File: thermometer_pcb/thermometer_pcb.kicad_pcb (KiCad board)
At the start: 2 copper layers, 76.6 x 49 mm, 18 parts, among them J1 POWER_IN, J2 TC_IN, J3 EXT_DS1, J4 EXT_DS2, J5 DISP, J6 Conn_01x02, Q1 PN2222A, U1 DS18B20

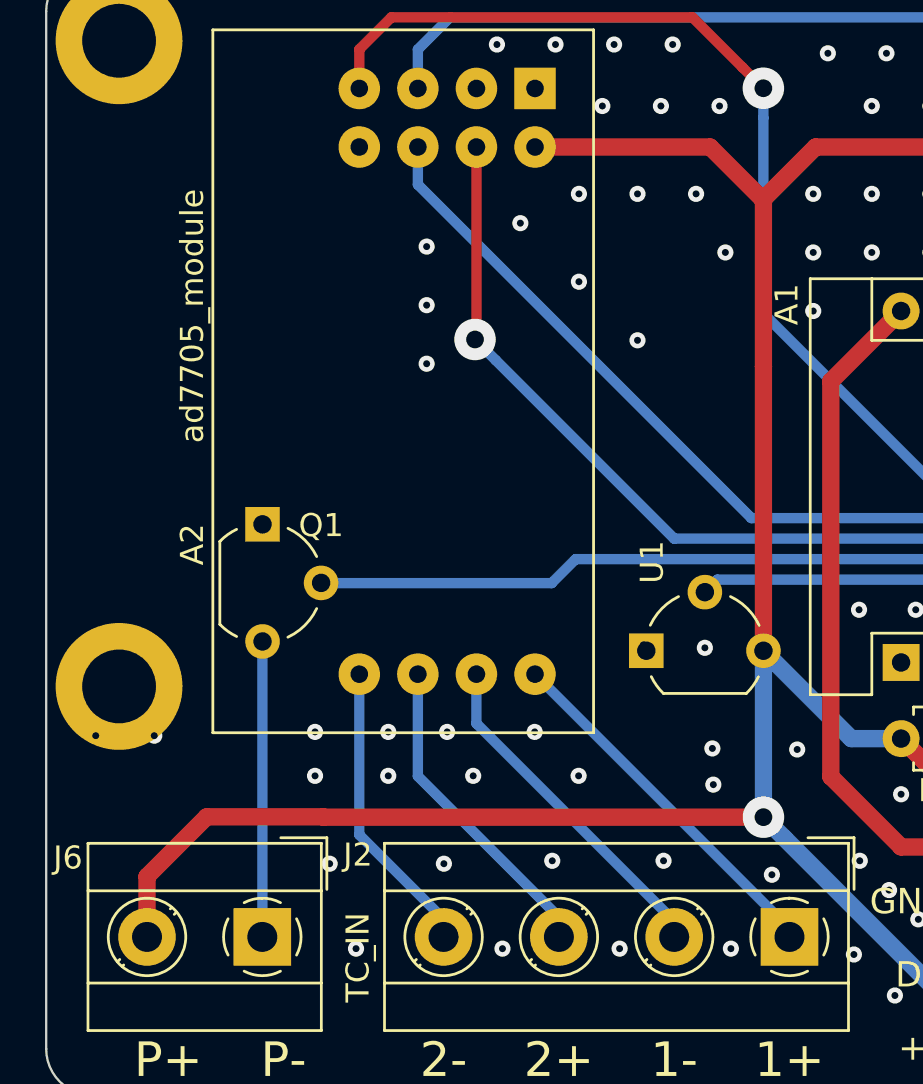
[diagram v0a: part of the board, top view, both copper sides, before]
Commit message: pcb: reroute PID+ track
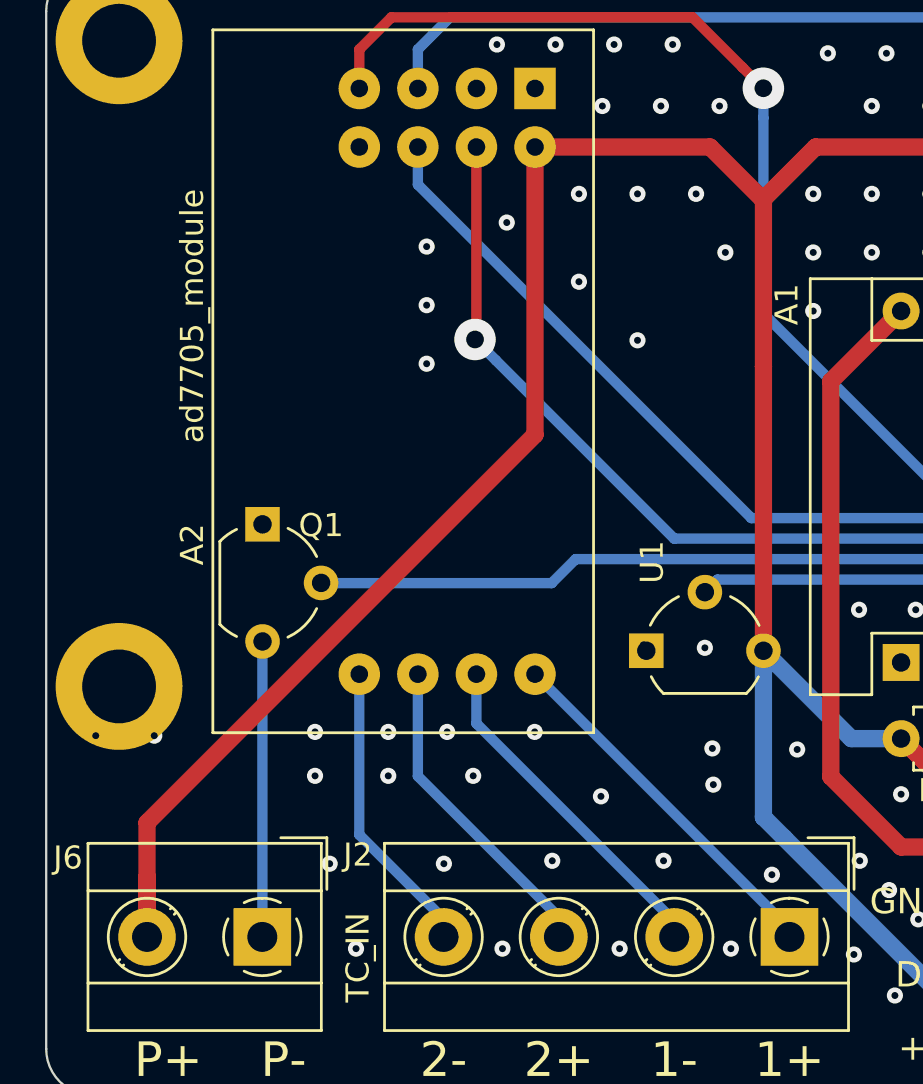
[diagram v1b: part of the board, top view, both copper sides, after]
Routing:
- net +5V: track 167.5 -> 180.9 mm, vias 1 -> 0
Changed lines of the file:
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@@
     (thickness 1.6)
     (drawings 60)
-    (tracks 272)
+    (tracks 270)
     (modules 18)
     (nets 20)
@@
   (gr_line (start 222.221676 76.190177) (end 222.221676 46.018604) (layer "Edge.Cuts") (width 0.1))
   (gr_arc (start 220.221676 46.018604) (end 222.221676 46.018604) (angle -90) (layer "Edge.Cuts") (width 0.1))
+  (segment (start 166.833677 64.382604) (end 150.008677 81.207604) (width 0.75) (layer "F.Cu") (net 2))
+  (segment (start 166.833677 51.906604) (end 166.833677 64.382604) (width 0.75) (layer "F.Cu") (net 2))
+  (segment (start 150.008677 81.207604) (end 150.008677 86.160604) (width 0.75) (layer "F.Cu") (net 2))
+  (via micro (at 169.693677 80.064604) (size 0.7) (drill 0.3) (layers "F.Cu" "B.Cu") (net 1))
+  (via micro (at 165.608667 55.182605) (size 0.7) (drill 0.3) (layers "F.Cu" "B.Cu") (net 1))
   (segment (start 199.208677 87.252604) (end 208.885477 77.575804) (width 0.45) (layer "B.Cu") (net 9))
   (segment (start 197.426677 87.252604) (end 199.208677 87.252604) (width 0.45) (layer "B.Cu") (net 9))
@@
   (segment (start 206.142677 86.102604) (end 202.299677 82.259604) (width 0.75) (layer "F.Cu") (net 5))
   (segment (start 179.660677 62.066604) (end 182.708677 59.018604) (width 0.75) (layer "F.Cu") (net 5))
-  (segment (start 157.661656 80.967625) (end 157.647635 80.953604) (width 0.75) (layer "F.Cu") (net 2))
-  (segment (start 157.647635 80.953604) (end 152.595677 80.953604) (width 0.75) (layer "F.Cu") (net 2))
   (segment (start 150.008677 83.540604) (end 150.008677 86.160604) (width 0.75) (layer "F.Cu") (net 2))
-  (segment (start 176.739698 80.967625) (end 157.661656 80.967625) (width 0.75) (layer "F.Cu") (net 2))
-  (segment (start 152.595677 80.953604) (end 150.008677 83.540604) (width 0.75) (layer "F.Cu") (net 2))
   (segment (start 155.012477 86.156804) (end 155.008677 86.160604) (width 0.45) (layer "B.Cu") (net 19))
   (segment (start 155.012477 73.353924) (end 155.012477 86.156804) (width 0.45) (layer "B.Cu") (net 19))
@@
   (segment (start 176.739677 80.967604) (end 176.739698 80.967625) (width 0.75) (layer "B.Cu") (net 2))
   (via micro (at 178.202677 78.032604) (size 0.7) (drill 0.3) (layers "F.Cu" "B.Cu") (net 1))
-  (via (at 176.739698 80.967625) (size 1.8) (drill 0.768) (layers "F.Cu" "B.Cu") (net 2))
   (via micro (at 174.566677 79.556604) (size 0.7) (drill 0.3) (layers "F.Cu" "B.Cu") (net 1))
   (via micro (at 164.152677 79.175604) (size 0.7) (drill 0.3) (layers "F.Cu" "B.Cu") (net 1))
   (via micro (at 160.469677 79.175604) (size 0.7) (drill 0.3) (layers "F.Cu" "B.Cu") (net 1))
-  (via micro (at 168.724677 79.175604) (size 0.7) (drill 0.3) (layers "F.Cu" "B.Cu") (net 1))
   (via micro (at 174.524732 77.986594) (size 0.7) (drill 0.3) (layers "F.Cu" "B.Cu") (net 1))
   (segment (start 176.739677 73.750604) (end 180.549677 77.560604) (width 0.75) (layer "B.Cu") (net 2))
@@
   (via micro (at 168.738677 57.748604) (size 0.7) (drill 0.3) (layers "F.Cu" "B.Cu") (net 1))
   (via micro (at 168.738677 53.938604) (size 0.7) (drill 0.3) (layers "F.Cu" "B.Cu") (net 1))
-  (via micro (at 166.198677 55.208604) (size 0.7) (drill 0.3) (layers "F.Cu" "B.Cu") (net 1))
   (via micro (at 175.088677 56.478604) (size 0.7) (drill 0.3) (layers "F.Cu" "B.Cu") (net 1))
   (via micro (at 186.518677 56.478604) (size 0.7) (drill 0.3) (layers "F.Cu" "B.Cu") (net 1))

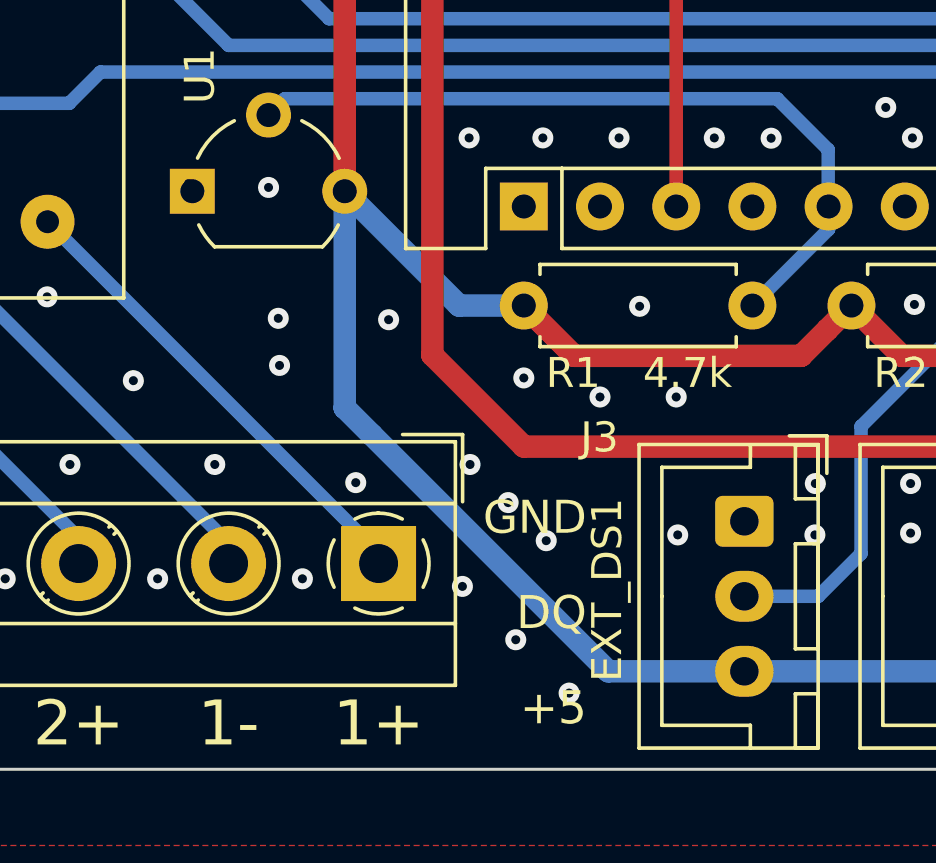
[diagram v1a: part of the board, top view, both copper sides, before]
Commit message: pcb: make +5V track shorter
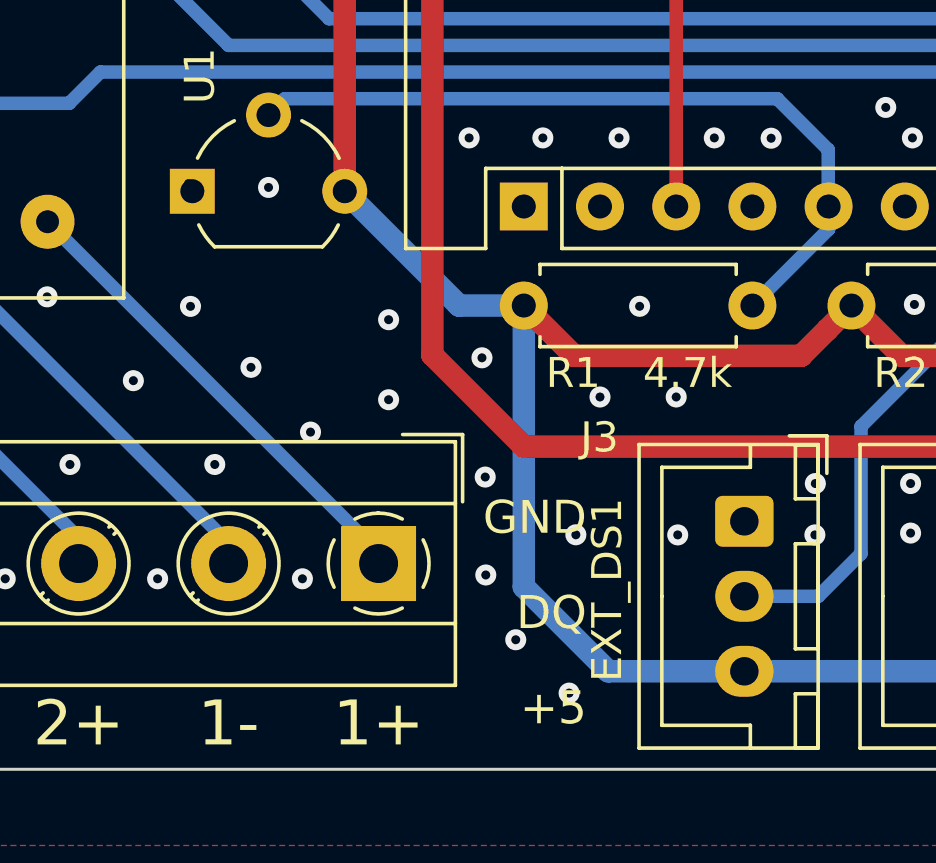
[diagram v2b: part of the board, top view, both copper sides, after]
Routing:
- net +5V: track 180.9 -> 174.7 mm

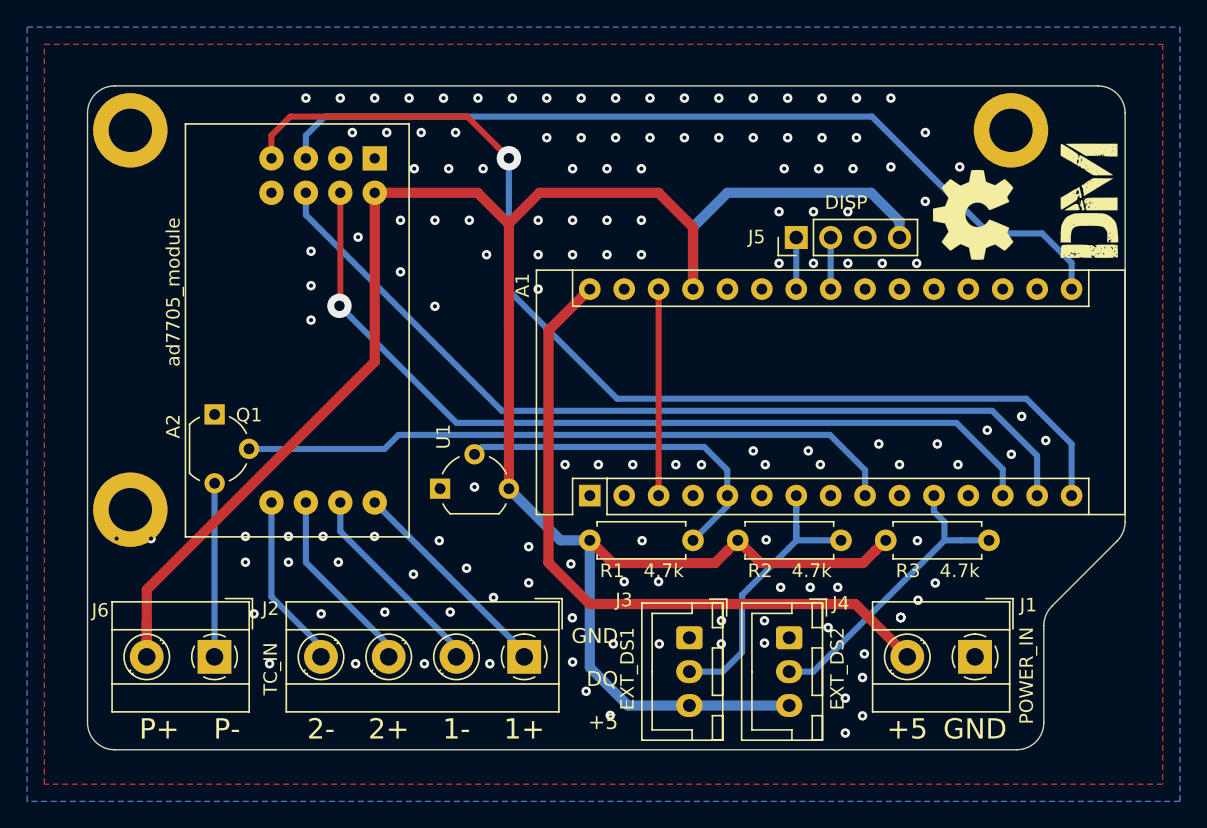
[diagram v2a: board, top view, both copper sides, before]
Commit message: pcb: reroute all nets; move resistors
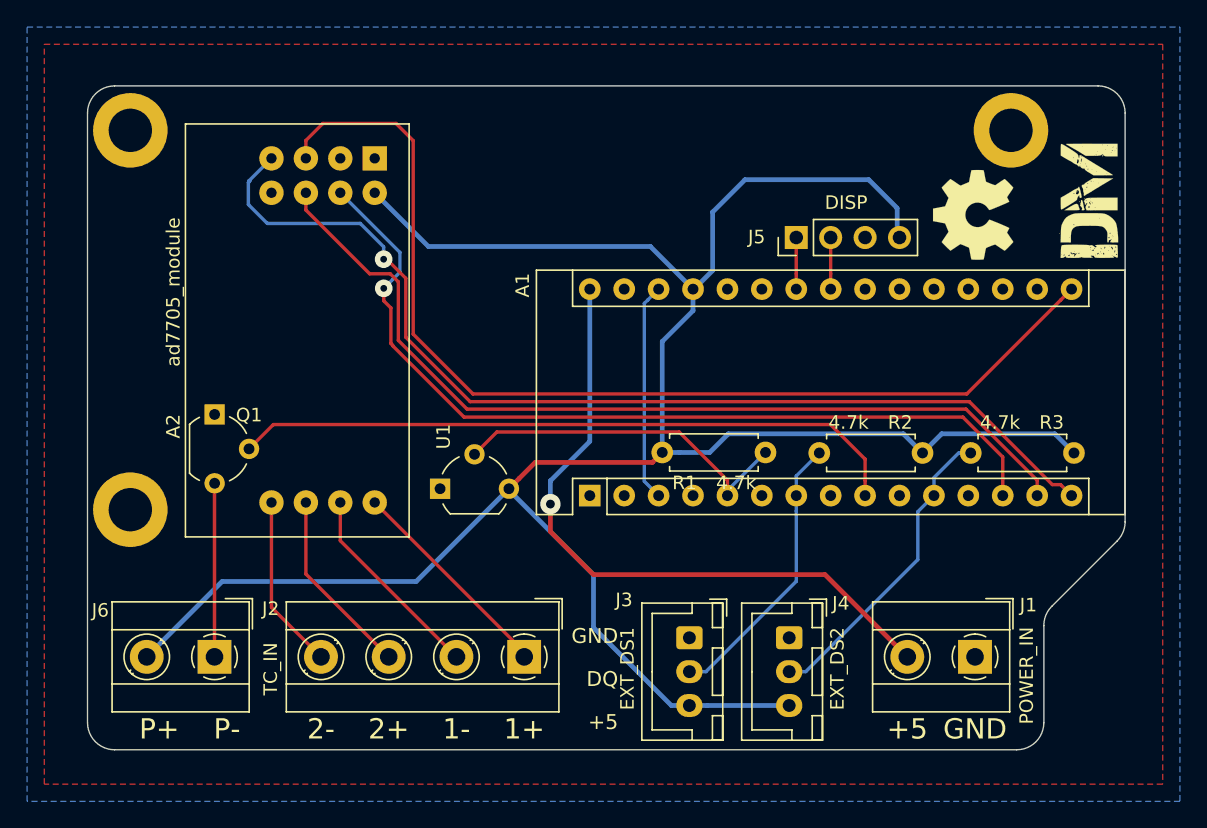
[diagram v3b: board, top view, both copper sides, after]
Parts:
- moved R3 15.3 mm to (218.4, 71.1), turned to 180 degrees
- moved R2 15.1 mm to (207.3, 71.1), turned to 180 degrees
- moved R1 8.41 mm to (188.1, 71.1)
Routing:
- net /13(SCK): track 65.2 -> 78.2 mm
- net +5V: track 174.7 -> 170.2 mm
- net /12(MISO): track 80.9 -> 77.0 mm
- net /4: track 23.1 -> 20.8 mm
- net /Vin: track 50.8 -> 49.3 mm, vias 0 -> 1
- net /11(**/MOSI): track 65.9 -> 67.2 mm
- net /6(**): track 48.9 -> 50.0 mm
- net /Reset: track 15.2 -> 16.1 mm
- net /10(**/SS): track 64.4 -> 65.2 mm
- net /8: track 22.4 -> 22.9 mm
- net GND: vias 147 -> 0
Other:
- net class Default: clearance 0.35 -> 0.3; trace_width 0.45 -> 0.25; via_dia 1.8 -> 1.3; via_drill 0.768 -> 0.5
- net class PWR: clearance 0.5 -> 0.4; trace_width 0.75 -> 0.35; via_dia 1.8 -> 1.5; via_drill 0.768 -> 0.65
- net class tc: clearance 0.5 -> 0.3; trace_width 0.75 -> 0.35; via_dia 1.8 -> 1.5; via_drill 0.768 -> 0.65
- rule trace_clearance: 0.35 -> 0.3

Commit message: pcb: add SPI pinheader
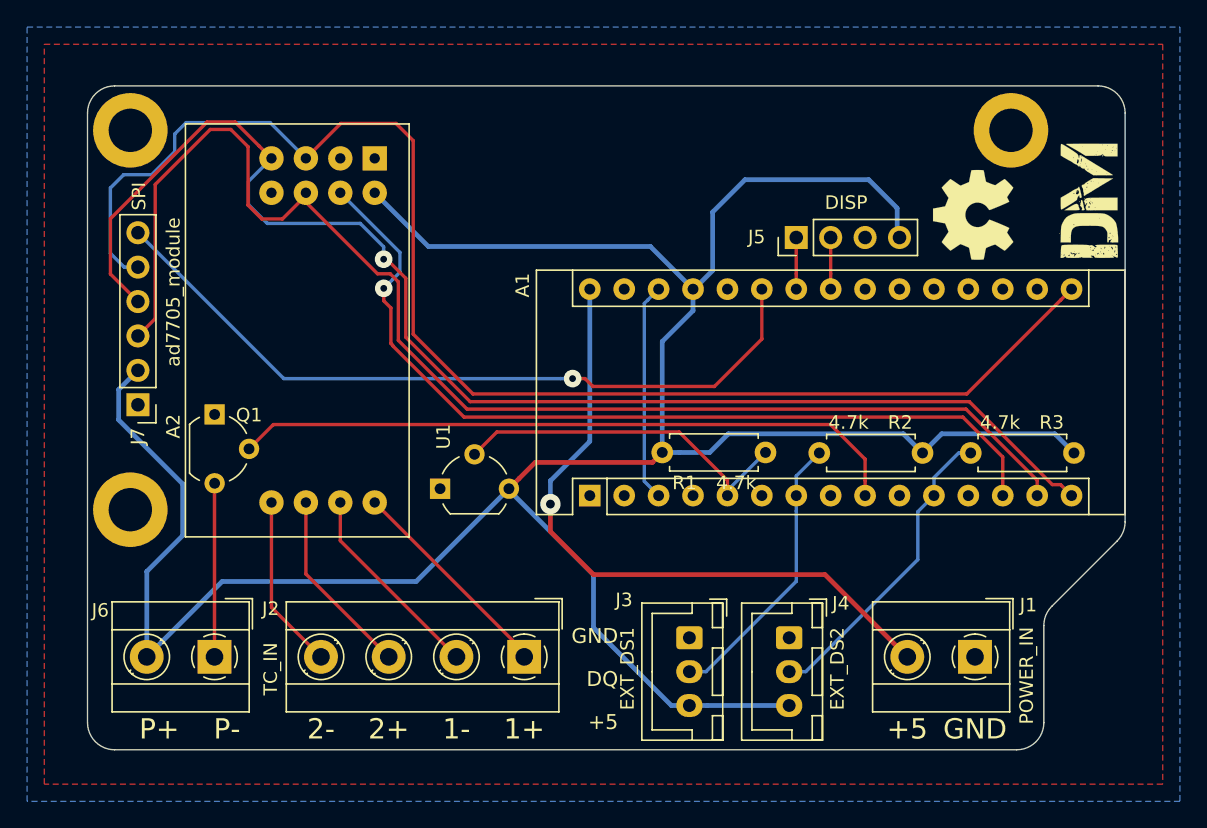
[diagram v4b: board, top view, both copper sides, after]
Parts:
- added J7: SPI, Connector_PinHeader_2.54mm:PinHeader_1x06_P2.54mm_Vertical, F.Cu at (149.4, 67.6)
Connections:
- A1 pad 25: (no net) -> /A6
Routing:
- net /A6: track 0.00 -> 55.9 mm, vias 0 -> 1
- net /11(**/MOSI): track 67.2 -> 97.8 mm
- net +5V: track 170.2 -> 195.0 mm
- net /13(SCK): track 78.2 -> 103.0 mm
- net /12(MISO): track 77.0 -> 99.8 mm
